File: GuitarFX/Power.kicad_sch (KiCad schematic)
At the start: 20 parts, among them J201 Jack-DC, U3 NCP718xSN500, U4 NCP1117-3.3_SOT223

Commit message: Created RGB LED footprint
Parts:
- D204: footprint (none) -> LED_SMD:LED_0603_1608Metric
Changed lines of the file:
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@@
       (effects (font (size 1.27 1.27)) (justify right))
     )
-    (property "Footprint" "" (at 172.085 109.22 0)
+    (property "Footprint" "LED_SMD:LED_0603_1608Metric" (at 172.085 109.22 0)
       (effects (font (size 1.27 1.27)) hide)
     )

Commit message: Assigned all footprints
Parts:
- removed J201: Jack-DC, symbol Connector:Jack-DC
- added J202: Screw_Terminal_01x02, TerminalBlock_Phoenix:TerminalBlock_Phoenix_MPT-0,5-2-2.54_1x02_P2.54mm_Horizontal, symbol Connector:Screw_Terminal_01x02
- FB302: footprint (none) -> Inductor_SMD:L_0603_1608Metric
- R201: footprint (none) -> TerminalBlock_Phoenix:TerminalBlock_Phoenix_MPT-0,5-6-2.54_1x06_P2.54mm_Horizontal
- R202: footprint (none) -> TerminalBlock_Phoenix:TerminalBlock_Phoenix_MPT-0,5-4-2.54_1x04_P2.54mm_Horizontal
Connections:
- net GND: now also J202.1 (Pin_1)
- net VCC: now also J202.2 (Pin_2)
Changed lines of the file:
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@@
-    (stroke (width 0) (type default))
-  )
-  (wire (pts (xy 60.96 62.865) (xy 62.23 62.865))
     (stroke (width 0) (type default))
   )
@@
     (stroke (width 0) (type default))
   )
+  (wire (pts (xy 54.61 62.865) (xy 62.23 62.865))
+    (stroke (width 0) (type default))
+  )
   (wire (pts (xy 118.11 115.57) (xy 133.35 115.57))
     (stroke (width 0) (type default))
@@
     (stroke (width 0) (type default))
   )
-  (wire (pts (xy 60.96 67.945) (xy 60.96 76.835))
+  (wire (pts (xy 60.96 65.405) (xy 60.96 76.835))
     (stroke (width 0) (type default))
   )
@@
     (stroke (width 0) (type default))
   )
+  (wire (pts (xy 54.61 65.405) (xy 60.96 65.405))
+    (stroke (width 0) (type default))
+  )
   (wire (pts (xy 191.135 73.025) (xy 191.135 75.565))
     (stroke (width 0) (type default))
@@
     (stroke (width 0) (type default))
   )
-  (rectangle (start 41.275 41.91) (end 214.63 124.46)
+  (rectangle (start 36.195 41.91) (end 214.63 124.46)
     (stroke (width 0) (type default))
     (fill (type none))
@@
   )
   (text "Input Filering, RP Protection, ESD Protection, Analog and Digital Supplies"
-    (at 41.275 41.275 0)
+    (at 35.56 41.275 0)
     (effects (font (size 2 2)) (justify left bottom))
   )
@@
       (effects (font (size 1.27 1.27)))
     )
-    (property "Footprint" "" (at 162.56 104.648 90)
+    (property "Footprint" "TerminalBlock_Phoenix:TerminalBlock_Phoenix_MPT-0,5-4-2.54_1x04_P2.54mm_Horizontal" (at 162.56 104.648 90)
       (effects (font (size 1.27 1.27)) hide)
     )
@@
       (effects (font (size 1.27 1.27)))
     )
-    (property "Footprint" "" (at 162.56 64.643 90)
+    (property "Footprint" "TerminalBlock_Phoenix:TerminalBlock_Phoenix_MPT-0,5-6-2.54_1x06_P2.54mm_Horizontal" (at 162.56 64.643 90)
       (effects (font (size 1.27 1.27)) hide)
     )
@@
         (path "/4ab4bfc6-98ca-4cb1-8273-436b96035b51/171d6b95-1f9c-4c9d-954a-bc461d0cb77a"
           (reference "R201") (unit 1)
-        )
-      )
-    )
-  )
-  (symbol (lib_id "Connector:Jack-DC") (at 53.34 65.405 0) (unit 1)
-    (in_bom yes) (on_board yes) (dnp no) (fields_autoplaced)
-    (property "Reference" "J201" (at 53.34 57.15 0)
-      (effects (font (size 1.27 1.27)))
-    )
-    (property "Value" "Jack-DC" (at 53.34 59.69 0)
-      (effects (font (size 1.27 1.27)))
-    )
-    (property "Footprint" "" (at 54.61 66.421 0)
-      (effects (font (size 1.27 1.27)) hide)
-    )
-    (property "Datasheet" "~" (at 54.61 66.421 0)
-      (effects (font (size 1.27 1.27)) hide)
-    )
-    (pin "1")
-    (pin "2")
-    (instances
-      (project "GuitarFX"
-        (path "/4ab4bfc6-98ca-4cb1-8273-436b96035b51/171d6b95-1f9c-4c9d-954a-bc461d0cb77a"
-          (reference "J201") (unit 1)
         )
       )
@@
       (effects (font (size 1.27 1.27)))
     )
-    (property "Footprint" "" (at 94.615 64.643 90)
+    (property "Footprint" "Inductor_SMD:L_0603_1608Metric" (at 94.615 64.643 90)
       (effects (font (size 1.27 1.27)) hide)
     )
@@
         )
       )
+    )
+  )
+  (symbol (lib_id "Connector:Screw_Terminal_01x02") (at 49.53 65.405 180) (unit 1)
+    (in_bom yes) (on_board yes) (dnp no)
+    (property "Reference" "J202" (at 48.895 72.39 0)
+      (effects (font (size 1.27 1.27)))
+    )
+    (property "Value" "Screw_Terminal_01x02" (at 49.53 69.85 0)
+      (effects (font (size 1.27 1.27)))
+    )
+    (property "Footprint" "TerminalBlock_Phoenix:TerminalBlock_Phoenix_MPT-0,5-2-2.54_1x02_P2.54mm_Horizontal" (at 49.53 65.405 0)
+      (effects (font (size 1.27 1.27)) hide)
+    )
+    (property "Datasheet" "~" (at 49.53 65.405 0)
+      (effects (font (size 1.27 1.27)) hide)
+    )
+    (pin "1")
+    (pin "2")
+    (instances
+      (project "GuitarFX"
+        (path "/4ab4bfc6-98ca-4cb1-8273-436b96035b51/171d6b95-1f9c-4c9d-954a-bc461d0cb77a"
+          (reference "J202") (unit 1)
+        )
+      )

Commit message: Fixed footprints for some components
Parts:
- R201: footprint TerminalBlock_Phoenix:TerminalBlock_Phoenix_MPT-0,5-6-2.54_1x06_P2.54mm_Horizontal -> Resistor_SMD:R_0603_1608Metric
- R202: footprint TerminalBlock_Phoenix:TerminalBlock_Phoenix_MPT-0,5-4-2.54_1x04_P2.54mm_Horizontal -> Resistor_SMD:R_0402_1005Metric
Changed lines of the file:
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@@
       (effects (font (size 1.27 1.27)))
     )
-    (property "Footprint" "TerminalBlock_Phoenix:TerminalBlock_Phoenix_MPT-0,5-4-2.54_1x04_P2.54mm_Horizontal" (at 162.56 104.648 90)
+    (property "Footprint" "Resistor_SMD:R_0402_1005Metric" (at 162.56 104.648 90)
       (effects (font (size 1.27 1.27)) hide)
     )
@@
       (effects (font (size 1.27 1.27)))
     )
-    (property "Footprint" "TerminalBlock_Phoenix:TerminalBlock_Phoenix_MPT-0,5-6-2.54_1x06_P2.54mm_Horizontal" (at 162.56 64.643 90)
+    (property "Footprint" "Resistor_SMD:R_0603_1608Metric" (at 162.56 64.643 90)
       (effects (font (size 1.27 1.27)) hide)
     )

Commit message: Changed butterworth filter components to 0603 for easier resoldering
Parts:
- R201: footprint Resistor_SMD:R_0603_1608Metric -> TerminalBlock_Phoenix:TerminalBlock_Phoenix_MPT-0,5-6-2.54_1x06_P2.54mm_Horizontal
- R202: footprint Resistor_SMD:R_0402_1005Metric -> TerminalBlock_Phoenix:TerminalBlock_Phoenix_MPT-0,5-4-2.54_1x04_P2.54mm_Horizontal
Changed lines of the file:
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@@
       (effects (font (size 1.27 1.27)))
     )
-    (property "Footprint" "Resistor_SMD:R_0402_1005Metric" (at 162.56 104.648 90)
+    (property "Footprint" "TerminalBlock_Phoenix:TerminalBlock_Phoenix_MPT-0,5-4-2.54_1x04_P2.54mm_Horizontal" (at 162.56 104.648 90)
       (effects (font (size 1.27 1.27)) hide)
     )
@@
       (effects (font (size 1.27 1.27)))
     )
-    (property "Footprint" "Resistor_SMD:R_0603_1608Metric" (at 162.56 64.643 90)
+    (property "Footprint" "TerminalBlock_Phoenix:TerminalBlock_Phoenix_MPT-0,5-6-2.54_1x06_P2.54mm_Horizontal" (at 162.56 64.643 90)
       (effects (font (size 1.27 1.27)) hide)
     )

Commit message: Corrected glitched old save for footprint assignment
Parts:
- R201: footprint TerminalBlock_Phoenix:TerminalBlock_Phoenix_MPT-0,5-6-2.54_1x06_P2.54mm_Horizontal -> Resistor_SMD:R_0603_1608Metric
- R202: footprint TerminalBlock_Phoenix:TerminalBlock_Phoenix_MPT-0,5-4-2.54_1x04_P2.54mm_Horizontal -> Resistor_SMD:R_0402_1005Metric
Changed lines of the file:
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@@
       (effects (font (size 1.27 1.27)))
     )
-    (property "Footprint" "TerminalBlock_Phoenix:TerminalBlock_Phoenix_MPT-0,5-4-2.54_1x04_P2.54mm_Horizontal" (at 162.56 104.648 90)
+    (property "Footprint" "Resistor_SMD:R_0402_1005Metric" (at 162.56 104.648 90)
       (effects (font (size 1.27 1.27)) hide)
     )
@@
       (effects (font (size 1.27 1.27)))
     )
-    (property "Footprint" "TerminalBlock_Phoenix:TerminalBlock_Phoenix_MPT-0,5-6-2.54_1x06_P2.54mm_Horizontal" (at 162.56 64.643 90)
+    (property "Footprint" "Resistor_SMD:R_0603_1608Metric" (at 162.56 64.643 90)
       (effects (font (size 1.27 1.27)) hide)
     )

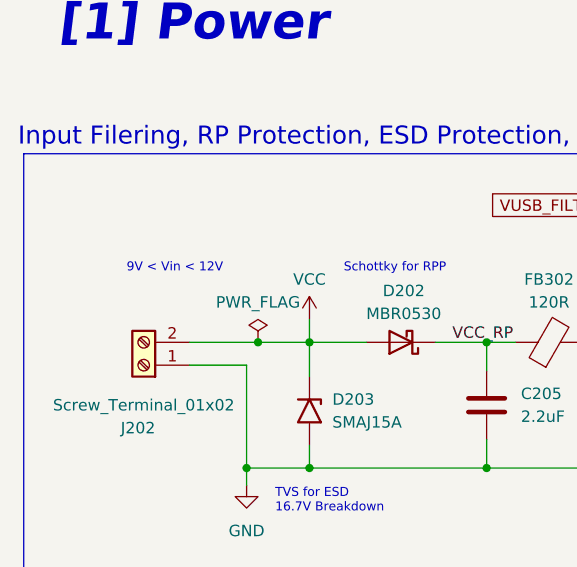
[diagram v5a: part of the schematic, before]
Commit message: Changed to mono input, and finished rough Analog Frontend layout
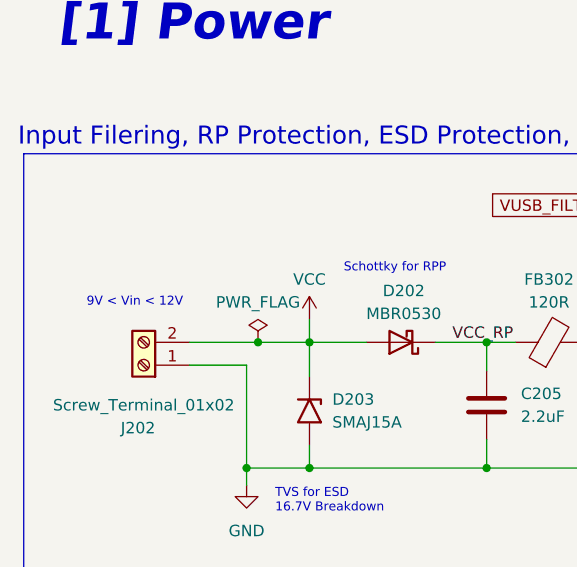
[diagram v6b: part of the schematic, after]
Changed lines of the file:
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@@
     (effects (font (size 2 2)) (justify left bottom))
   )
-  (text "9V < Vin < 12V" (at 47.625 55.245 0)
+  (text "9V < Vin < 12V" (at 43.18 59.055 0)
     (effects (font (size 1 1)) (justify left bottom))
   )

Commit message: Finished rough layout
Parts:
- R201: footprint Resistor_SMD:R_0603_1608Metric -> Resistor_SMD:R_0805_2012Metric
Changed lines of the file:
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@@
       (effects (font (size 1.27 1.27)))
     )
-    (property "Footprint" "Resistor_SMD:R_0603_1608Metric" (at 162.56 64.643 90)
+    (property "Footprint" "Resistor_SMD:R_0805_2012Metric" (at 162.56 64.643 90)
       (effects (font (size 1.27 1.27)) hide)
     )
